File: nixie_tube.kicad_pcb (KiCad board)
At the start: 2 copper layers, 25.8 x 56.3 mm, 28 parts, among them J1 Conn_01x06_Male, J11 dc003a, J2 Conn_01x06_Female, J3 Conn_01x01_Male, J4 Conn_01x01_Female, Q1 SS8550, Q2 FQD5N60C, Q3 Q_NPN_BCE, Q4 TP0610T, U1 MC34063

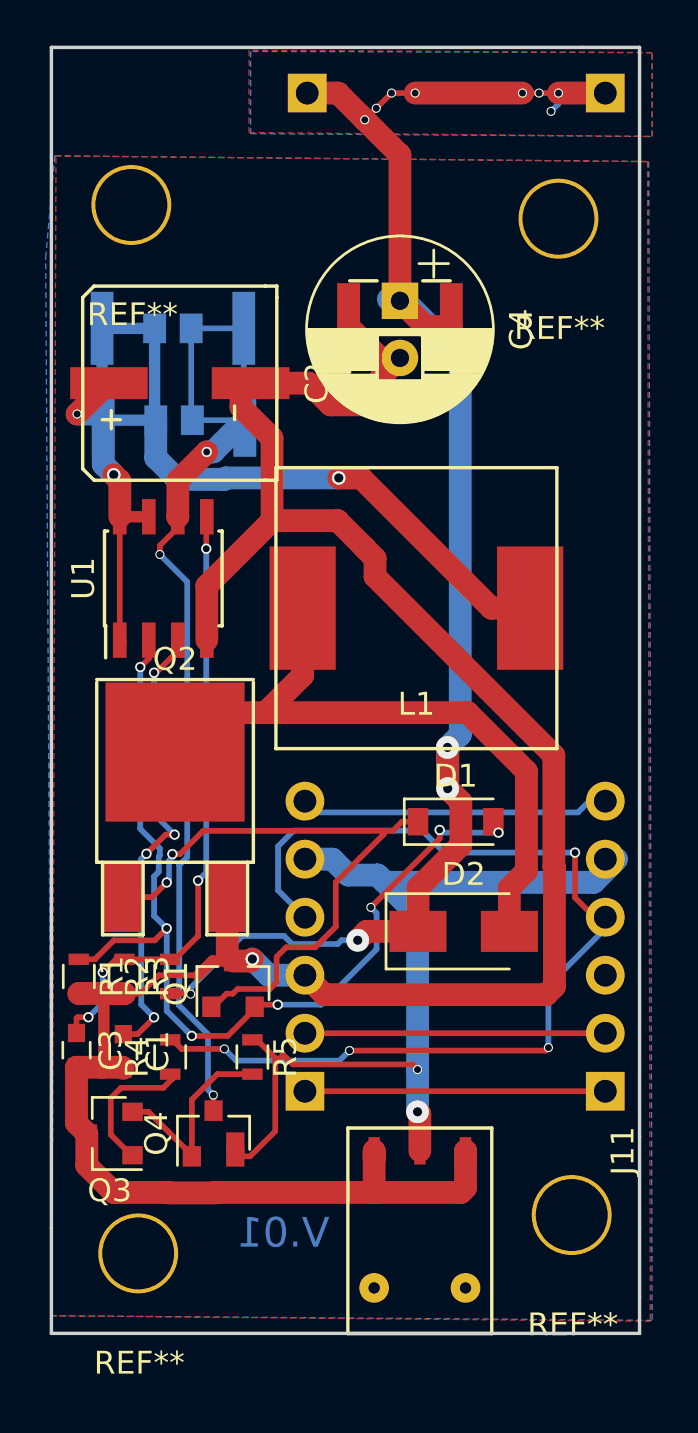
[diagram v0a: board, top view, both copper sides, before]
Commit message: fixed pin position for ss8500
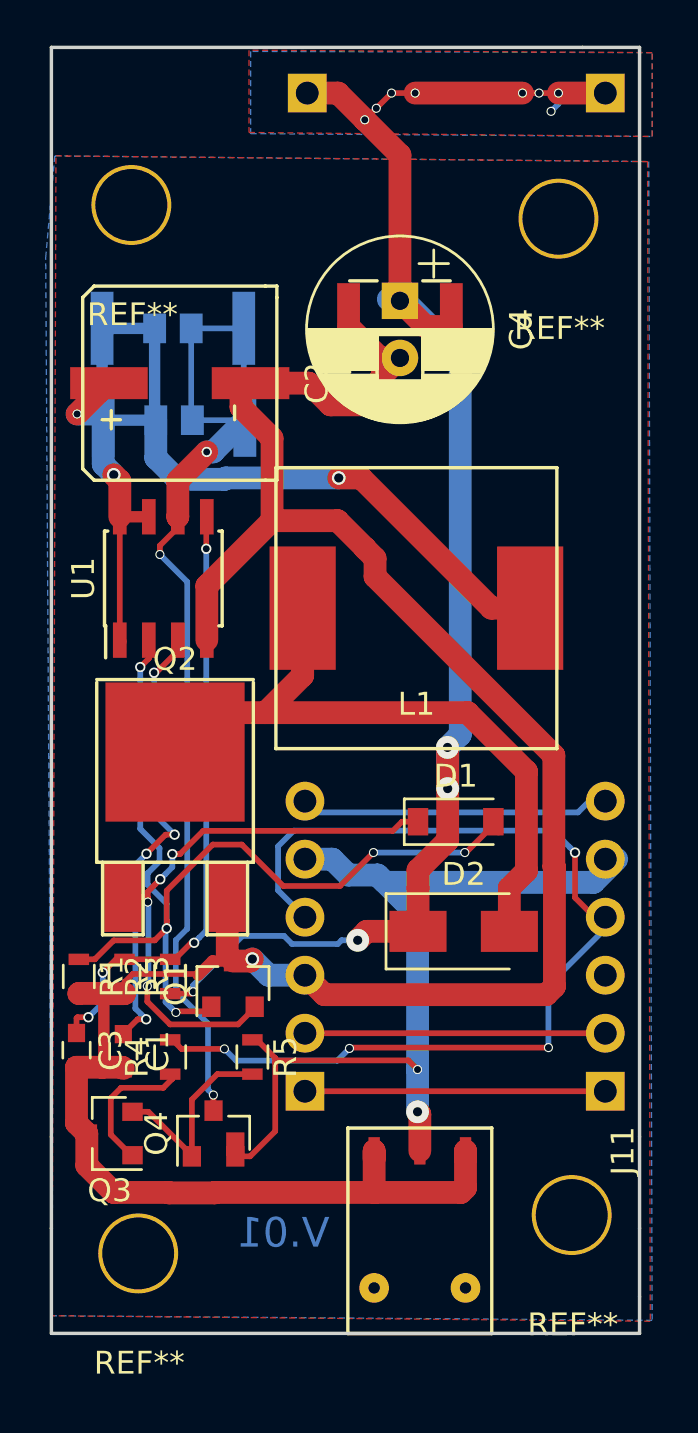
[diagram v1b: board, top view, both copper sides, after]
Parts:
- Q1: value SS8550 -> Q_PNP_BEC
- Q4: value TP0610T -> AO3407
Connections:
- Q1 pad 1: Net-(D1-Pad1) -> Net-(D1-Pad2)
- Q1 pad 2: Net-(D1-Pad2) -> Net-(D1-Pad1)
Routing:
- net Net-(D1-Pad1): track 27.4 -> 25.5 mm, vias 2 -> 4
- net Net-(D1-Pad2): track 42.8 -> 43.0 mm, vias 7 -> 5

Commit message: fixed npn pin numbering not same with real device
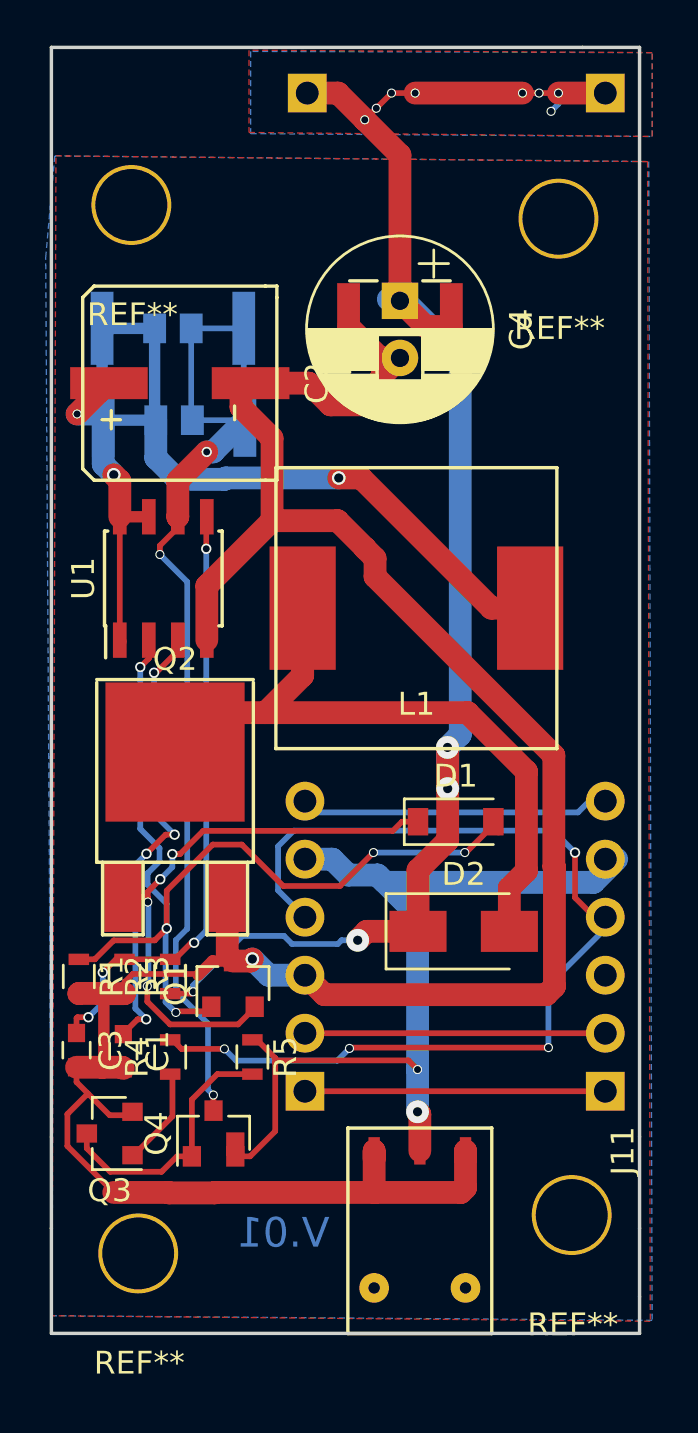
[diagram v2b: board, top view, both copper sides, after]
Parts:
- Q1: value Q_PNP_BEC -> SS8550
- Q3: value Q_NPN_BCE -> MMBTA42LT1
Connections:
- Q3 pad 2: Net-(Q3-Pad2) -> GND
- Q3 pad 3: GND -> Net-(Q3-Pad3)
- Q4 pad 1: Net-(Q3-Pad2) -> Net-(Q3-Pad3)
- R5 pad 2: Net-(Q3-Pad2) -> Net-(Q3-Pad3)
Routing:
- net Net-(Q3-Pad3): track 0.00 -> 11.6 mm
- net Net-(Q3-Pad2): track 9.03 -> 0.00 mm
- net GND: track 108.5 -> 111.7 mm
- net Net-(Q3-Pad1): track 6.17 -> 4.30 mm

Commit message: fixed correct footprint for pin headers and socket, removed silk screen
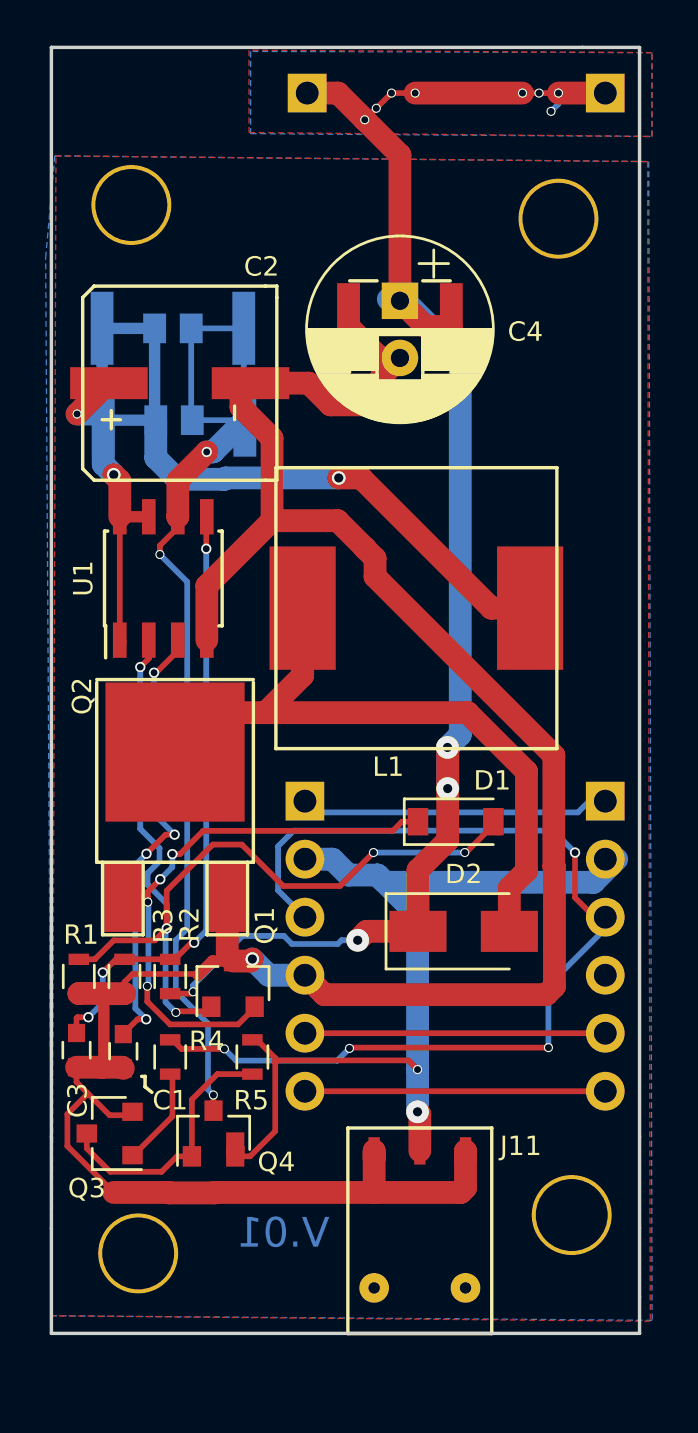
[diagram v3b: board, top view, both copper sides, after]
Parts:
- J1: footprint Pin_Headers:Pin_Header_Angled_1x06_Pitch2.54mm -> nixie-tube-fp:Socket_Strip_Angled_1x06_Pitch2.54mm_without_slikscreen
- J2: footprint Socket_Strips:Socket_Strip_Angled_1x06_Pitch2.54mm -> Pin_Headers:Pin_Header_Angled_1x06_Pitch2.54mm
- J4: footprint Socket_Strips:Socket_Strip_Angled_1x01_Pitch2.54mm -> nixie-tube-fp:Socket_Strip_Angled_1x01_Pitch2.54mm_without_silkScreen
- moved J1 12.7 mm to (190.8, 112.8), turned to 180 degrees
- moved J2 12.7 mm to (177.6, 112.8), turned to 180 degrees
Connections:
- J1 pad 1: /MOSi -> /STORE
- J1 pad 2: /SCK -> +VDC
- J1 pad 3: GND -> /PWREN
- J1 pad 4: /PWREN -> GND
- J1 pad 5: +VDC -> /SCK
- J1 pad 6: /STORE -> /MOSi
- J2 pad 1: /MOSi -> /STORE
- J2 pad 2: /SCK -> +VDC
- J2 pad 3: GND -> /PWREN
- J2 pad 4: /PWREN -> GND
- J2 pad 5: +VDC -> /SCK
- J2 pad 6: /STORE -> /MOSi
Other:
- board text added: "GND"
- board text added: "HV"
- board text added: "MOSI"
- board text added: "PWREN"
- board text added: "SCK"
- board text added: "STORE"
- board text added: "VDC"
